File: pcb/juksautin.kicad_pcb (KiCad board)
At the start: 2 copper layers, 65 x 35 mm, 26 parts, among them J1 Screw_Terminal_01x09, J3 AVR-ISP-6, J4 Conn_01x09, U1 SP3485EN, U2 SRV05-4, U3 R-78E5.0-0.5, U4 ATmega328P-AU, Y1 X322516MLB4SI

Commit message: pcb: Add debug header for serial comm, reduce unique capacitor count by 1
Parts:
- added J2: Serial_Debug, Connector_PinHeader_1.27mm:PinHeader_1x04_P1.27mm_Vertical, F.Cu at (129.5, 78.8)
- C2: footprint Capacitor_SMD:C_0402_1005Metric -> Capacitor_SMD:C_1206_3216Metric
- moved C2 5.23 mm to (166.5, 81.0)
- moved C3 4.90 mm to (161.6, 81.0)
- moved U1 1.51 mm to (134.8, 77.2)
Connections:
- C2 pad 1: VCC -> VIN
- C3 pad 1: VIN -> VCC
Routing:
- net /RX: track 14.3 -> 19.3 mm
- net VCC: track 103.8 -> 99.6 mm
- net /TX_EN: track 10.7 -> 12.5 mm
- net /TX: track 8.59 -> 10.3 mm

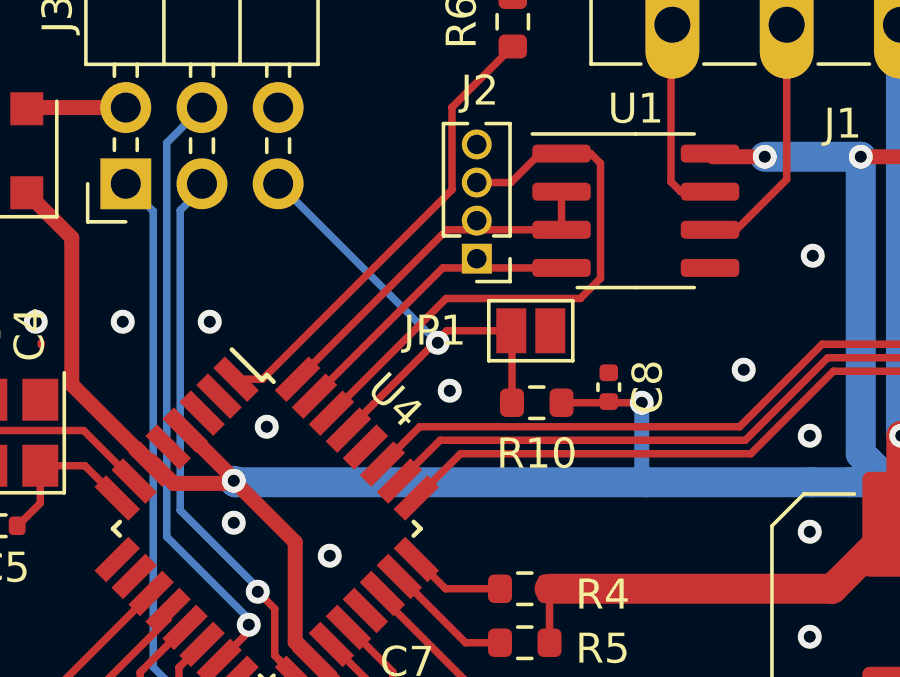
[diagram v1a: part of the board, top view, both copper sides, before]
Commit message: pcb: Remove reset pad (we have header anyway) and and RX pull-up
RX pull-up seems to be required to keep RX HIGH during transmit phase
when SP3485 is HI-Z.
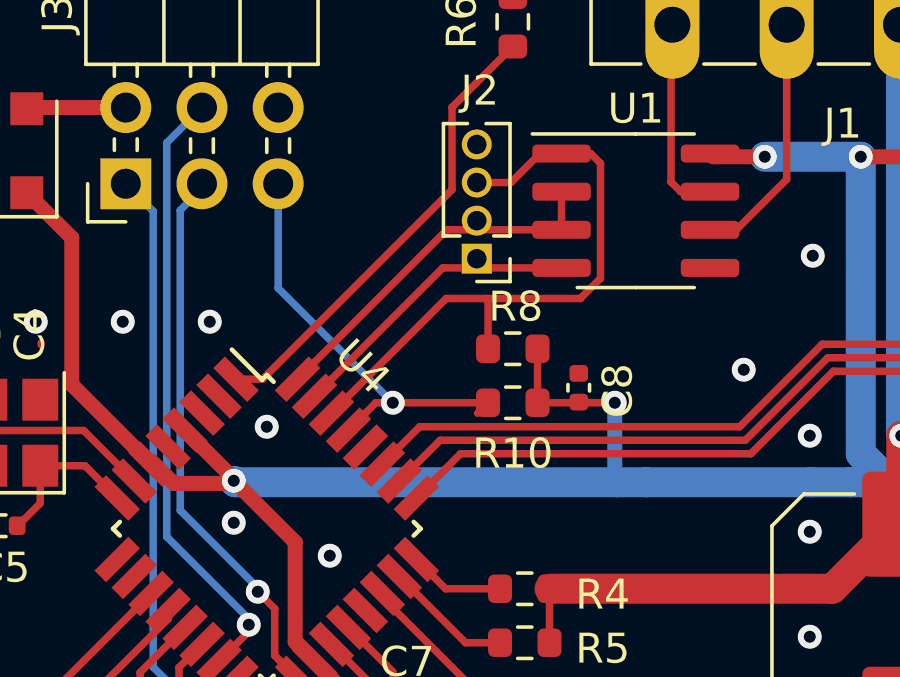
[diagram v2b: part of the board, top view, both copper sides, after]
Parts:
- removed JP1: Reset pad, Jumper:SolderJumper-2_P1.3mm_Open_Pad1.0x1.5mm
- added R8: 10k, Resistor_SMD:R_0603_1608Metric, F.Cu at (130.7, 81.8)
- moved C8 1.00 mm to (132.9, 83.1)
- moved R10 0.80 mm to (130.7, 83.6)
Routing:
- net /RX: track 19.3 -> 21.2 mm
- net VCC: track 99.6 -> 101.3 mm
- net /RESET: track 16.9 -> 15.4 mm
- net GND: vias 17 -> 16

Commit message: pcb: Some changes. Don't remember anymore.
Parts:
- R8: value 10k -> 20k
- moved U1 0.92 mm to (135.7, 77.2)
- moved J2 0.67 mm to (130.1, 79.1)
- moved R8 0.10 mm to (130.7, 81.9)
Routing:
- net /RX: track 21.2 -> 16.3 mm, vias 0 -> 1
- net VCC: track 101.3 -> 103.4 mm
- net PUMPFAIL: track 23.9 -> 23.0 mm
- net B: track 7.32 -> 7.96 mm
- net Net-(R6-Pad2): track 15.4 -> 14.9 mm

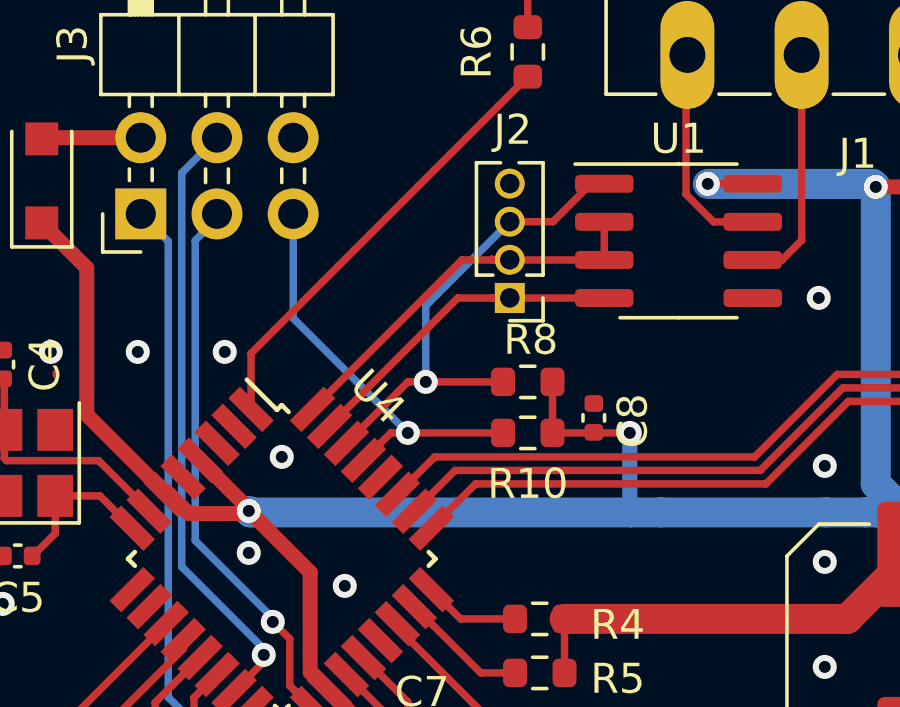
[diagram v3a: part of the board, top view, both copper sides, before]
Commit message: pcb: Remove extra hole-trough from RX line
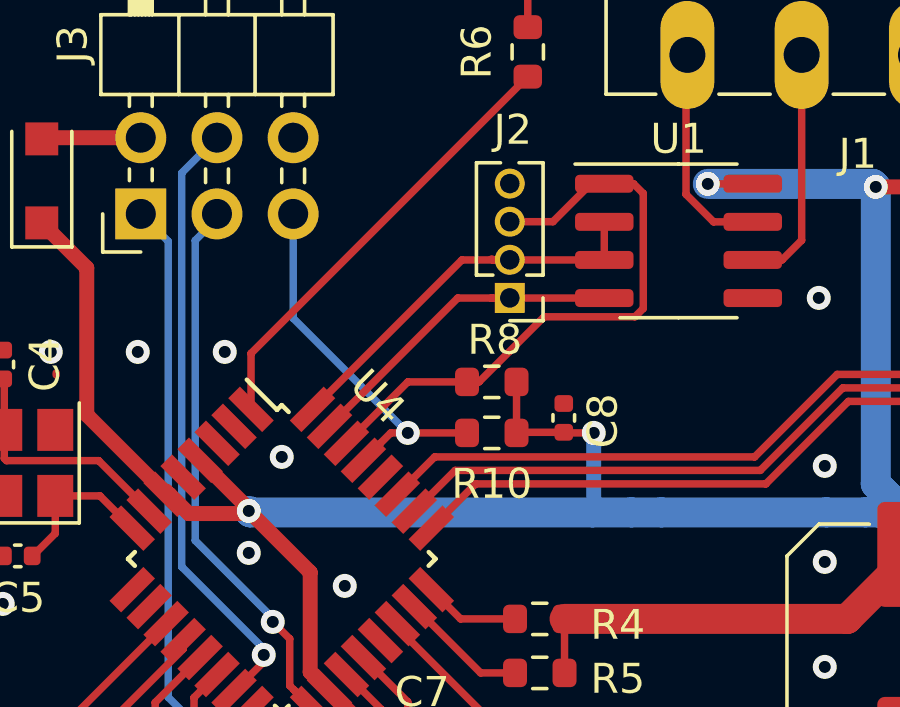
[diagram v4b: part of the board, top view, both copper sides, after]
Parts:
- moved R10 1.20 mm to (129.5, 83.6)
- moved R8 1.20 mm to (129.5, 81.9)
- moved C8 1.00 mm to (131.9, 83.1)
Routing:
- net /RX: track 16.3 -> 20.7 mm, vias 1 -> 0
- net /RESET: track 14.9 -> 13.7 mm
